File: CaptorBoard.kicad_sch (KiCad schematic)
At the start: 51 parts, among them J1 Conn_01x06, J2 Screw_Terminal_01x03, J3 Screw_Terminal_01x03, J4 Conn_01x07, J5 Conn_01x04, J6 Screw_Terminal_01x03, K1 G5LE-1-DC5, K2 G5LE-1-DC5, Q1 2N7002E, Q2 2N7002E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

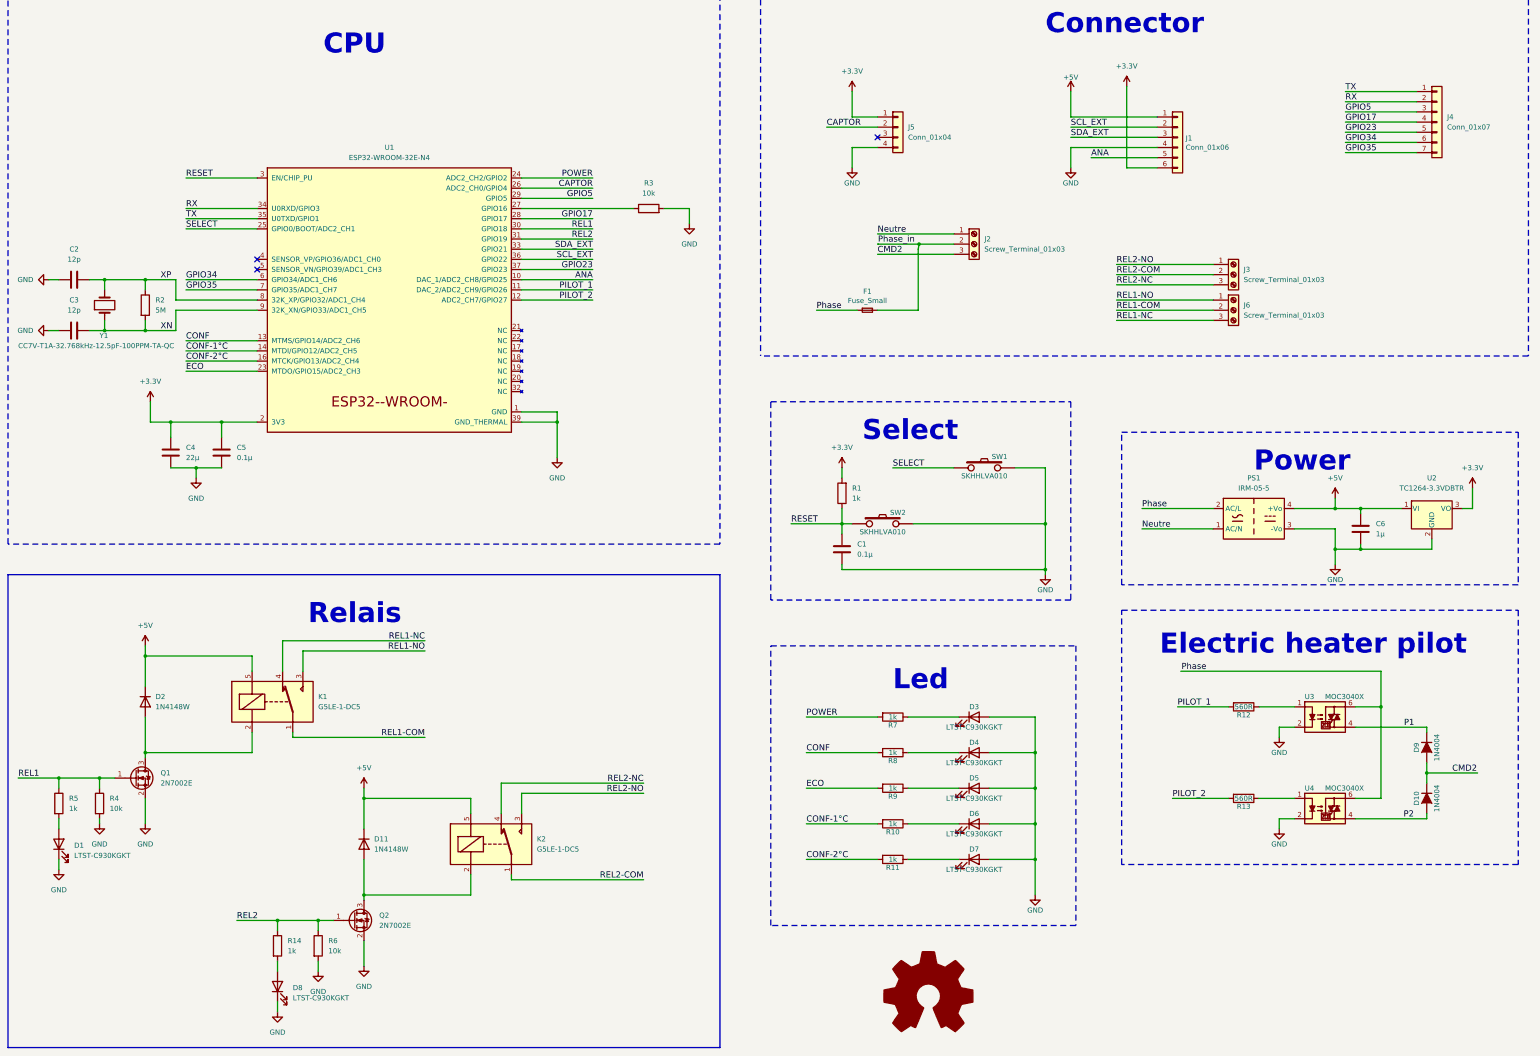
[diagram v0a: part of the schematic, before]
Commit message: Change AC/DC converter for one smaller and chiper
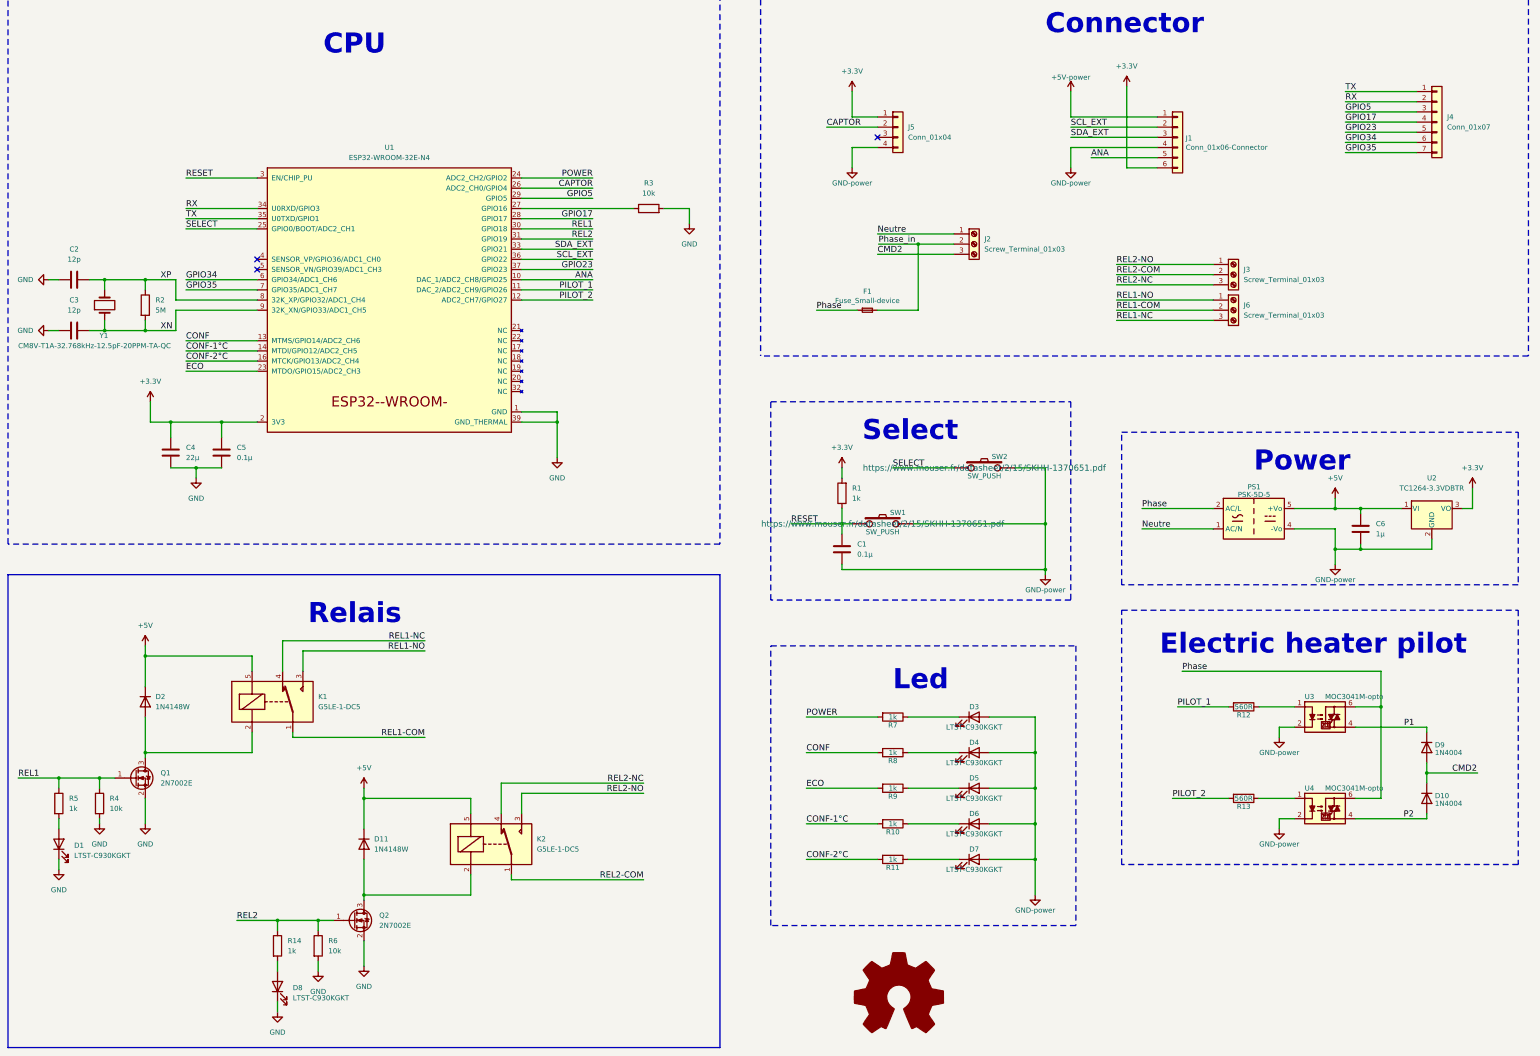
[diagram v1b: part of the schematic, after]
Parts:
- removed D10, D9: 1N4004, Diode_THT:D_DO-41_SOD81_P7.62mm_Horizontal, symbol CaptorBoard-rescue:D-RESCUE-CaptorBoard
- removed LOGO1: Logo_Open_Hardware_Large, Symbol:OSHW-Logo_11.4x12mm_SilkScreen, symbol Graphic:Logo_Open_Hardware_Large
- removed PS1: IRM-05-5, Converter_ACDC:Converter_ACDC_MeanWell_IRM-05-xx_THT, symbol Converter_ACDC:IRM-05-5
- added D10, D9: 1N4004, Diode_THT:D_DO-41_SOD81_P7.62mm_Horizontal, symbol Diode:1N4004
- added PS1: PSK-5D-5, pfo:PSK5D5, symbol pfo:PSK-5D-5
- added SYM1: Logo_Open_Hardware_Large, Symbol:OSHW-Logo2_14.6x12mm_SilkScreen, symbol Graphic:Logo_Open_Hardware_Large
- C1, C5: manf# (none) -> 12101C104K4T2A
- C2, C3: manf# (none) -> C1210C120J1HACTU
- C4: manf# (none) -> CL32A226MOJNNNE
- C6: manf# (none) -> CL32B105KBHNNNE
- D1, D3, D4, D5, D6, D7, D8: manf# (none) -> LTST-C930KGKT
- D11, D2: manf# (none) -> 1N4148W-E3-08
- F1: value Fuse_Small -> Fuse_Small-device; manf# (none) -> 0443001.DR
- J1: value Conn_01x06 -> Conn_01x06-Connector; now left out of the parts list
- J2, J3, J6: manf# (none) -> TB007-508-03BE
- J4, J5: now left out of the parts list
- K1, K2: manf# (none) -> G5LE-1-DC5
- Q1, Q2: manf# (none) -> 2N7002KT1G
- R1, R10, R11, R14, R5, R7, R8, R9: manf# (none) -> RMC1/4-102JTE
- R12, R13: manf# (none) -> RK73B2ETTD561J
- R2: manf# (none) -> CRMA1210AF4M99FKEF
- R3, R4, R6: manf# (none) -> RMCF1210FT10K0
- SW1: renamed from SW2; value SKHHLVA010 -> SW_PUSH; manf# (none) -> SKHHLPA010
- SW2: renamed from SW1; value SKHHLVA010 -> SW_PUSH; manf# (none) -> SKHHLPA010
- U1: manf# (none) -> ESP32-WROOM-32E-N4
- U2: manf# (none) -> TC1264-3.3VDBTR
- U3, U4: value MOC3040X -> MOC3041M-opto; manf# (none) -> MOC3041VM
- Y1: value CC7V-T1A-32.768kHz-12.5pF-100PPM-TA-QC -> CM8V-T1A-32.768kHz-12.5pF-20PPM-TA-QC; footprint Crystal:Crystal_SMD_MicroCrystal_CC7V-T1A-2Pin_3.2x1.5mm_HandSoldering -> Crystal:Crystal_SMD_MicroCrystal_CC8V-T1A-2Pin_2.0x1.2mm_HandSoldering; manf# (none) -> CM8V-T1A-32.768kHz-12.5pF-20PPM-TA-QC
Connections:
- net +5V: now also PS1.5 (+Vo)
- net CMD2: now also D10.1 (K), D9.2 (A)
- net GND: now also PS1.4 (-Vo)
- net Neutre: now also PS1.1 (AC/N)
- net P1: now also D9.1 (K)
- net P2: now also D10.2 (A)
- net Phase: now also PS1.2 (AC/L)

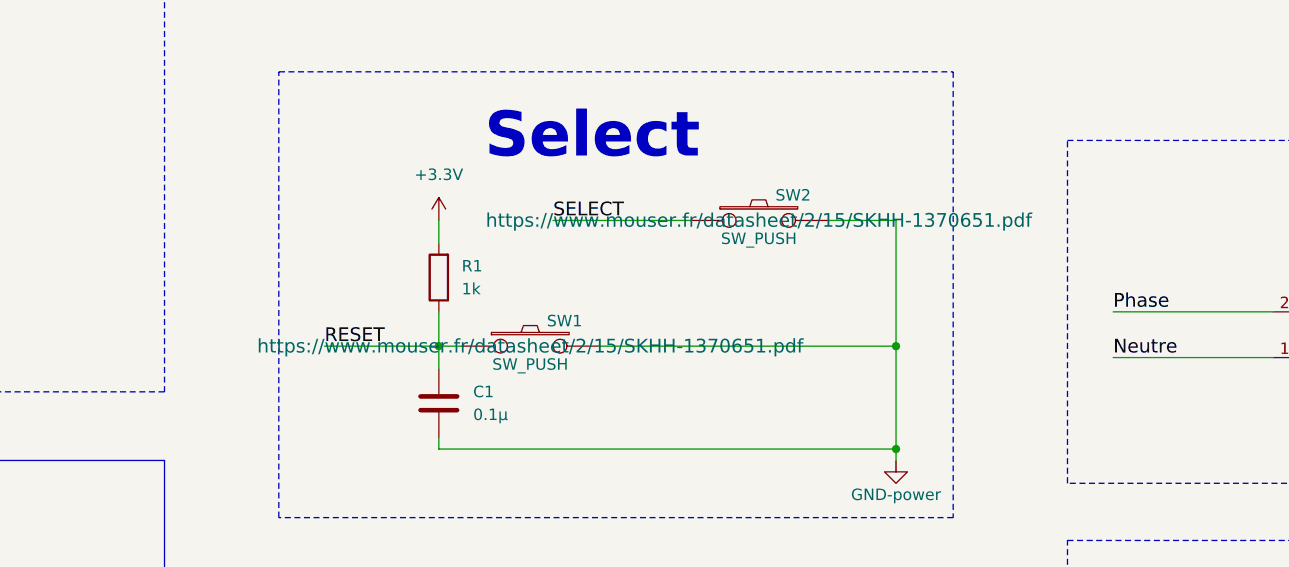
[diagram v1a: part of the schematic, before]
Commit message: Change somme manufacturer referance
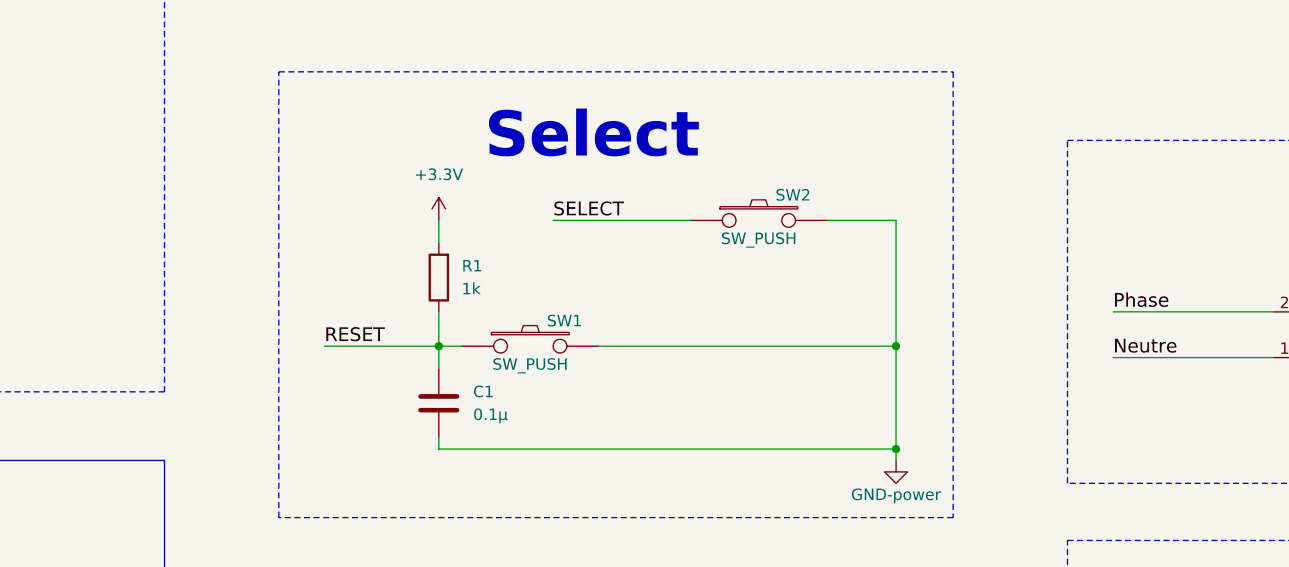
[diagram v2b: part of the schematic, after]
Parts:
- Q1, Q2: manf# 2N7002KT1G -> 2N7002E-7-F
- U3, U4: manf# MOC3041VM -> MOC3041M
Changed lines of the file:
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@@
     )
     (property "Datasheet" "https://www.mouser.fr/datasheet/2/15/SKHH-1370651.pdf" (at 264.16 135.89 0)
-      (effects (font (size 1.524 1.524)))
+      (effects (font (size 1.524 1.524)) hide)
     )
     (property "manf#" "SKHHLPA010" (at 264.16 135.89 0)
@@
     )
     (property "Datasheet" "https://www.mouser.fr/datasheet/2/15/SKHH-1370651.pdf" (at 238.76 149.86 0)
-      (effects (font (size 1.524 1.524)))
+      (effects (font (size 1.524 1.524)) hide)
     )
     (property "manf#" "SKHHLPA010" (at 238.76 149.86 0)
@@
       (effects (font (size 1.27 1.27)) (justify left) hide)
     )
-    (property "manf#" "MOC3041VM" (at 349.25 198.12 0)
+    (property "manf#" "MOC3041M" (at 349.25 198.12 0)
       (effects (font (size 1.27 1.27)) hide)
     )
@@
       (effects (font (size 1.27 1.27)) (justify left) hide)
     )
-    (property "manf#" "MOC3041VM" (at 349.25 220.98 0)
+    (property "manf#" "MOC3041M" (at 349.25 220.98 0)
       (effects (font (size 1.27 1.27)) hide)
     )
@@
       (effects (font (size 1.27 1.27)) (justify left) hide)
     )
-    (property "manf#" "2N7002KT1G" (at 106.68 248.92 0)
+    (property "manf#" "2N7002E-7-F" (at 106.68 248.92 0)
       (effects (font (size 1.27 1.27)) hide)
     )
@@
       (effects (font (size 1.27 1.27)) (justify left) hide)
     )
-    (property "manf#" "2N7002KT1G" (at 52.07 213.36 0)
-      (effects (font (size 1.27 1.27)) hide)
-    )
+    (property "manf#" "2N7002E-7-F" (at 52.07 213.36 0)
+      (effects (font (size 1.27 1.27)) hide)
+    )

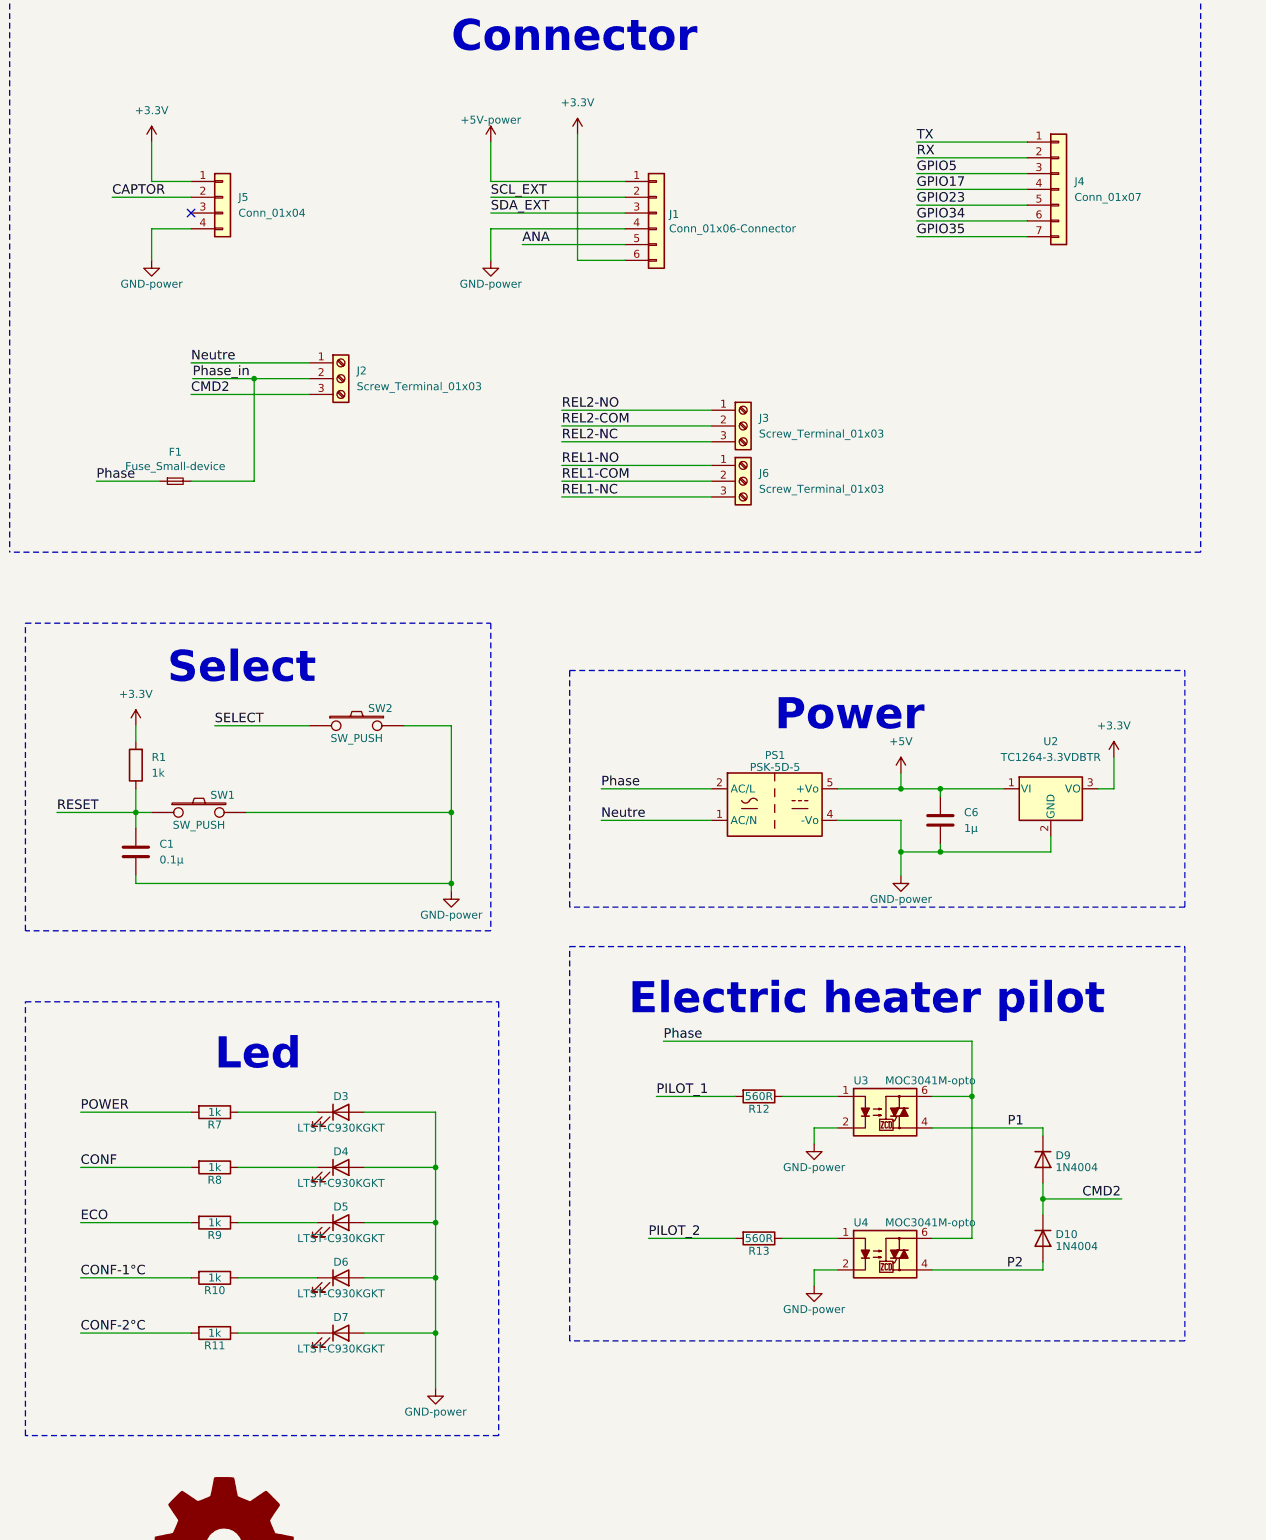
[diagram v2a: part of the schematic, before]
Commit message: change power label name because their are not the same
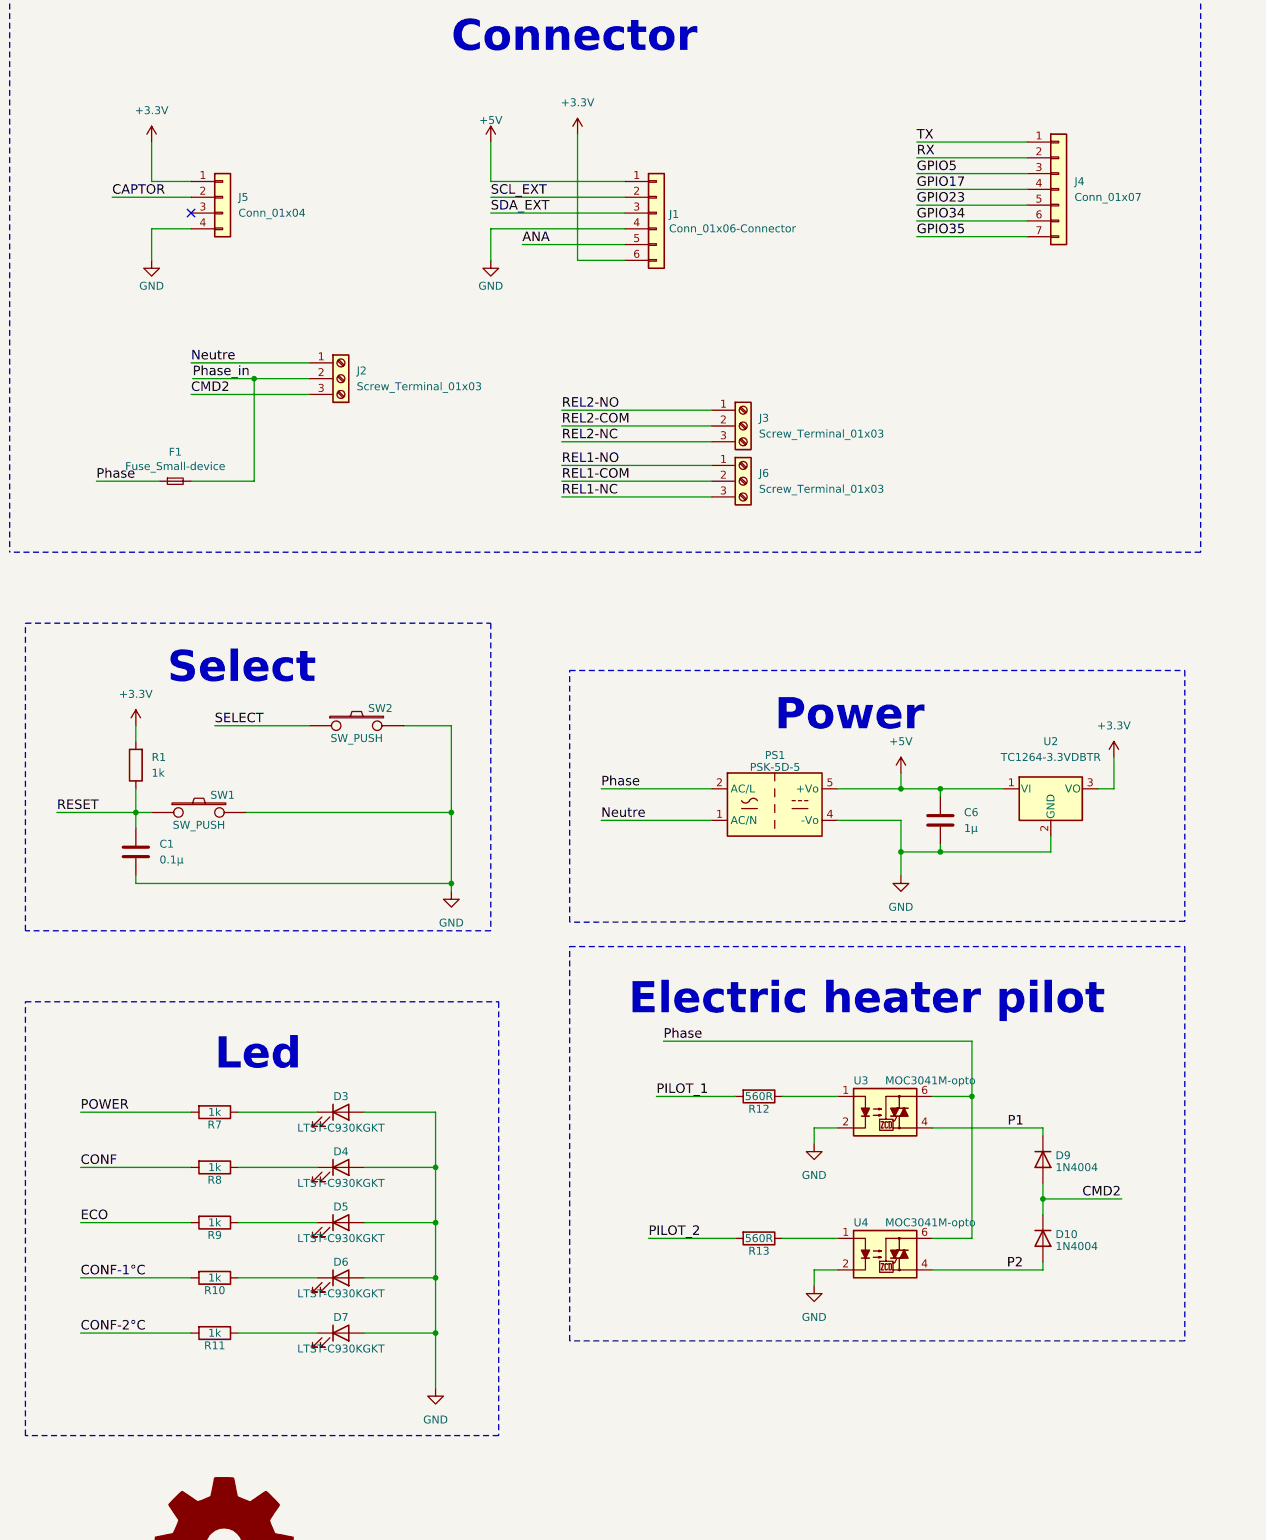
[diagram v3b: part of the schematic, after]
